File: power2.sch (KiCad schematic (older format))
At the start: 42 parts, among them U3 LMS6002DR2, U4 ECP5

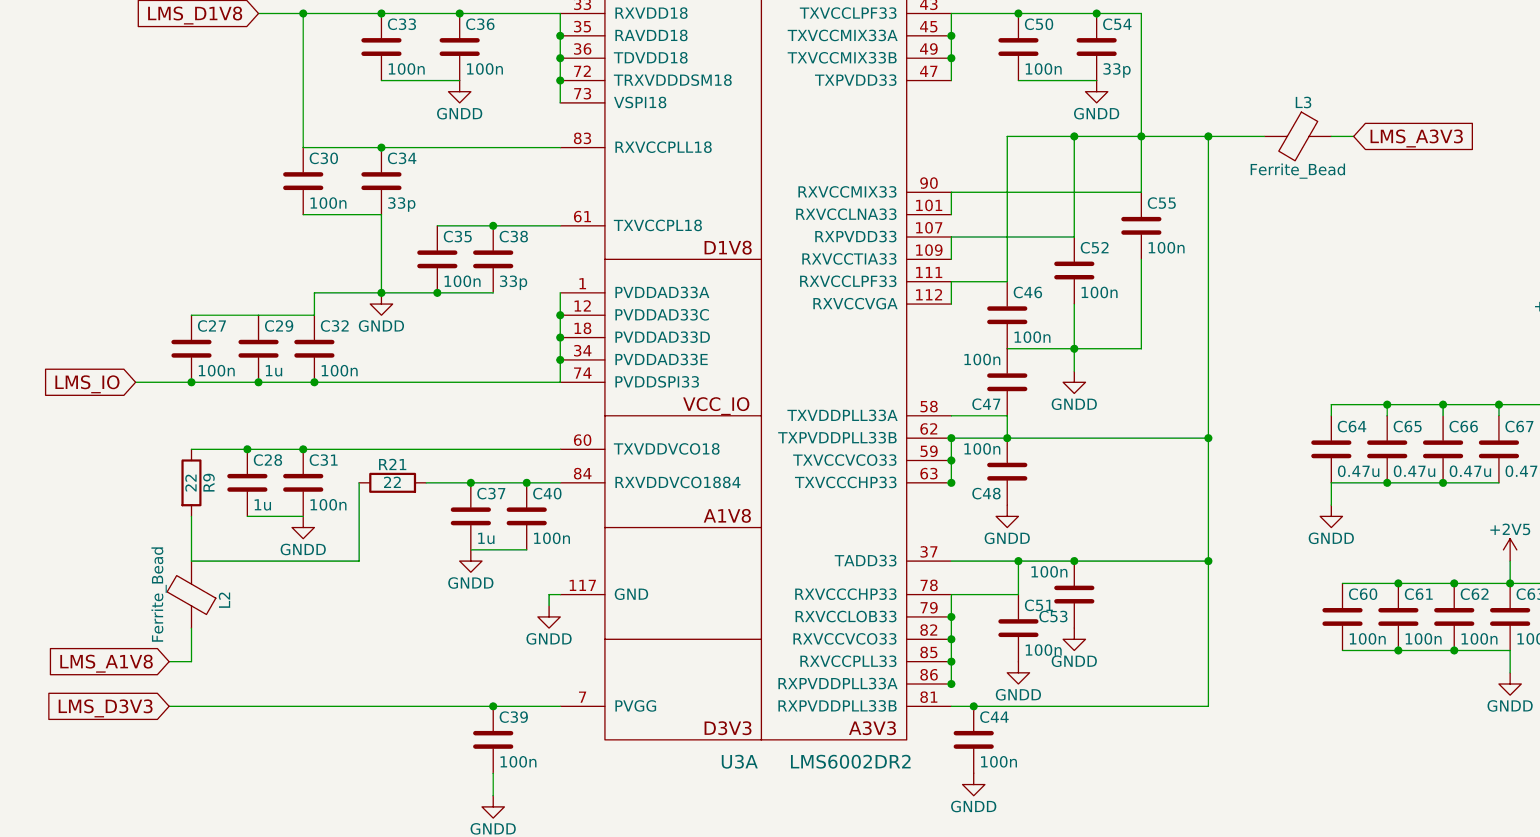
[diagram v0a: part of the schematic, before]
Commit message: Placed most components for FTDI. Begin tracing FT601
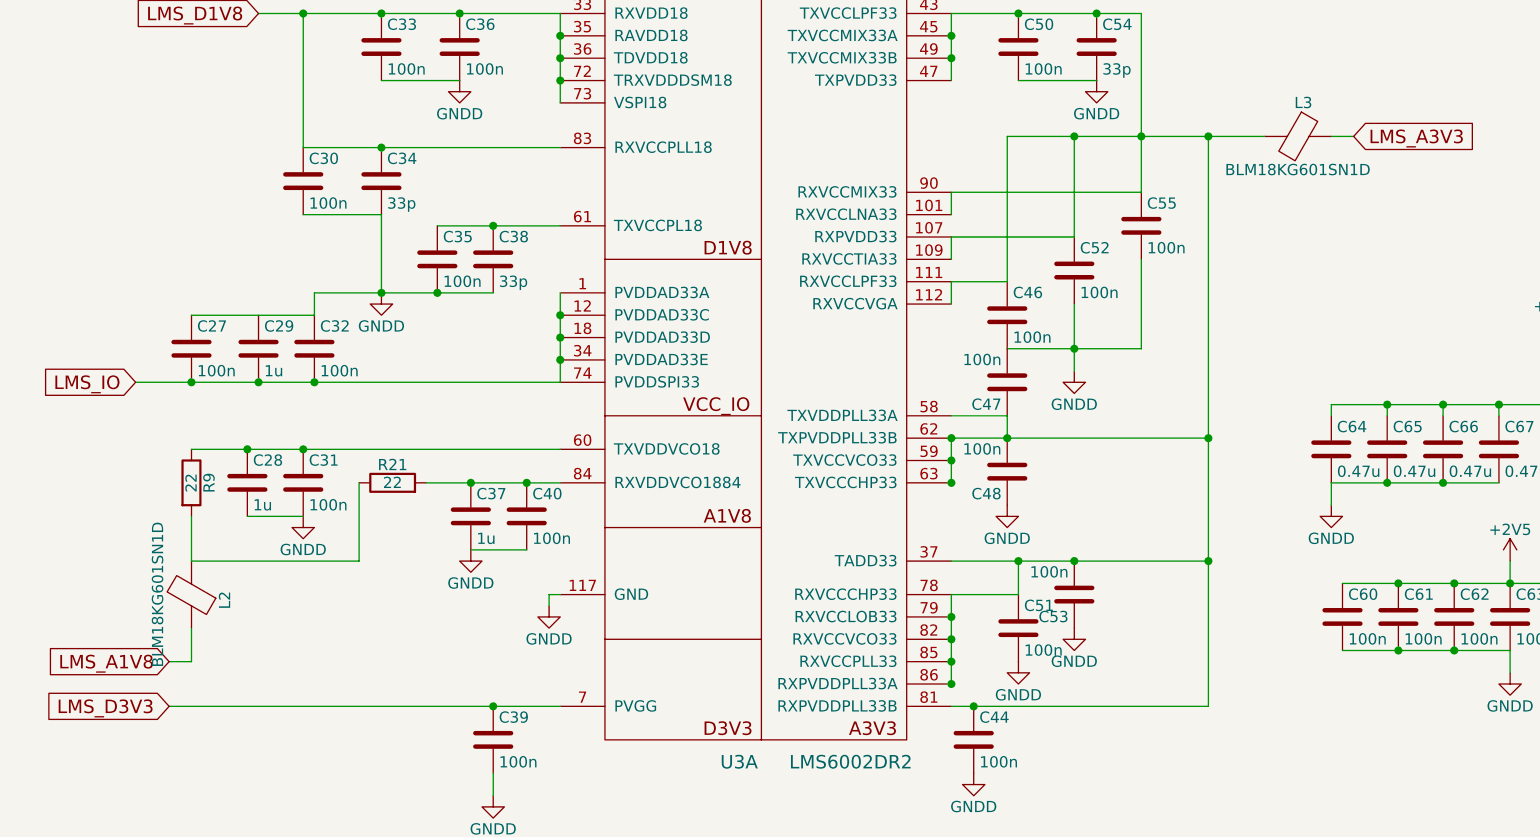
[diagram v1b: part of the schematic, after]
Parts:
- C27, C28, C29, C30, C31, C32, C33, C34, C35, C36, C37, C38, C39, C40, C44, C46, C47, C48, C50, C51, C52, C53, C54, C55, C60, C61, C62, C63, C64, C65, C66, C67, C68, C69, C70, C71: footprint Capacitors_SMD:C_0402 -> Capacitors_SMD:C_0603
- L2, L3: value Ferrite_Bead -> BLM18KG601SN1D; footprint Inductors_SMD:L_0603_HandSoldering -> Capacitors_SMD:C_0805
- R21, R9: footprint Resistors_SMD:R_0402 -> Resistors_SMD:R_0603

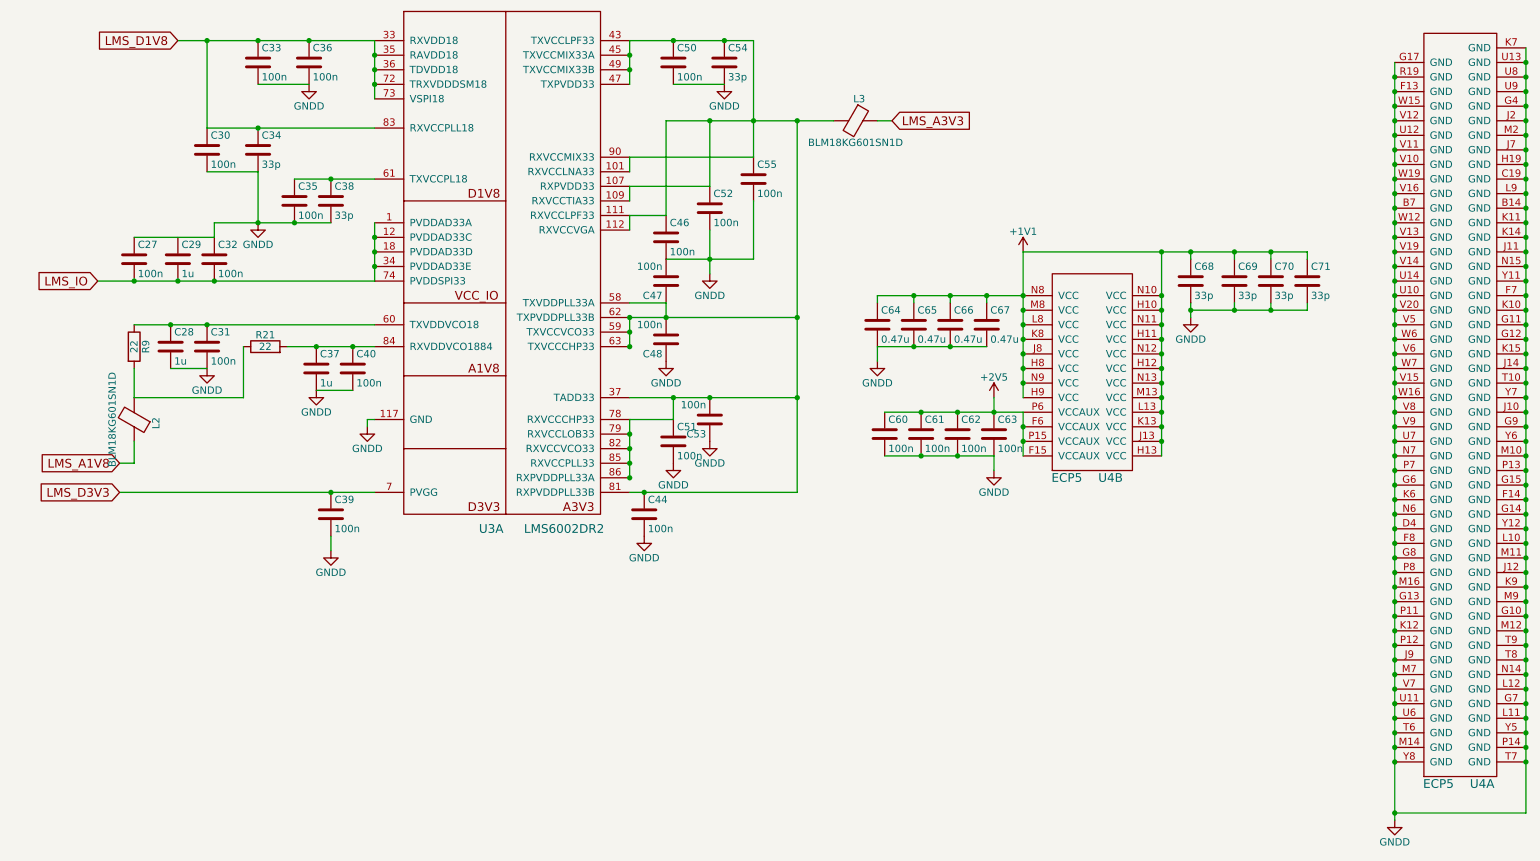
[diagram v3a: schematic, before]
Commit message: Start placing RF. Shield is ready. Fixed some net bugs.
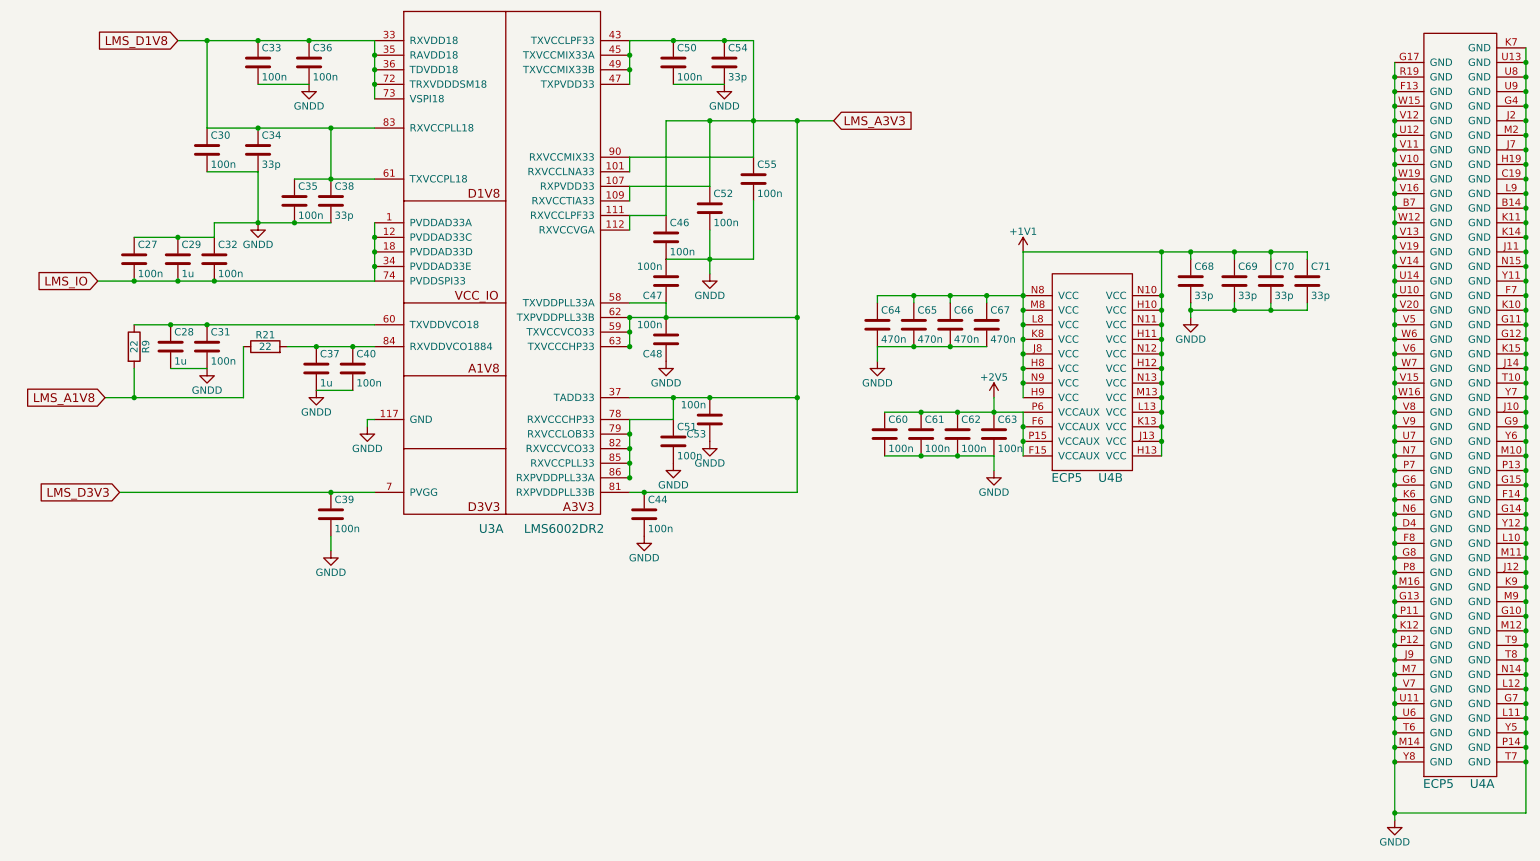
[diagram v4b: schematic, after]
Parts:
- removed L2, L3: BLM18KG601SN1D, Capacitors_SMD:C_0805, symbol Ferrite_Bead
- C64, C65, C66, C67: value 0.47u -> 470n
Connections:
- net GNDD: now also C29.1
- net LMS_A1V8: now also R21.1, R9.2
- net LMS_A3V3: now also C44.1, C46.1, C47.1, C48.2, C50.1, C51.1, C52.1, C53.2, C54.1, C55.1, U3.101 (RXVCCLNA33), U3.107 (RXPVDD33), U3.109 (RXVCCTIA33), U3.111 (RXVCCLPF33), U3.112 (RXVCCVGA), U3.37 (TADD33), U3.43 (TXVCCLPF33), U3.45 (TXVCCMIX33A), U3.47 (TXPVDD33), U3.49 (TXVCCMIX33B), U3.58 (TXVDDPLL33A), U3.59 (TXVCCVCO33), U3.62 (TXPVDDPLL33B), U3.63 (TXVCCCHP33), U3.78 (RXVCCCHP33), U3.79 (RXVCCLOB33), U3.81 (RXPVDDPLL33B), U3.82 (RXVCCVCO33), U3.85 (RXVCCPLL33), U3.86 (RXPVDDPLL33A), U3.90 (RXVCCMIX33)
- net LMS_D1V8: now also C35.1, C38.1, U3.61 (TXVCCPL18)
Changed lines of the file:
@@
 Connection ~ 10950 1000
 $Comp
-L GNDD #PWR058
+L GNDD #PWR067
 U 1 1 58A3CB56
 P 10050 6200
-F 0 "#PWR058" H 10050 5950 50  0001 C CNN
+F 0 "#PWR067" H 10050 5950 50  0001 C CNN
 F 1 "GNDD" H 10050 6050 50  0000 C CNN
 F 2 "" H 10050 6200 50  0000 C CNN
@@
 $EndComp
 $Comp
-L +1V1 #PWR059
+L +1V1 #PWR068
 U 1 1 58A3D047
 P 7500 2300
-F 0 "#PWR059" H 7500 2150 50  0001 C CNN
+F 0 "#PWR068" H 7500 2150 50  0001 C CNN
 F 1 "+1V1" H 7500 2440 50  0000 C CNN
 F 2 "" H 7500 2300 50  0000 C CNN
@@
 $EndComp
 $Comp
-L C C32
-U 1 1 58A43C54
-P 1950 2350
-F 0 "C32" H 1975 2450 50  0000 L CNN
-F 1 "100n" H 1975 2250 50  0000 L CNN
-F 2 "Capacitors_SMD:C_0603" H 1988 2200 50  0001 C CNN
-F 3 "" H 1950 2350 50  0000 C CNN
-	1    1950 2350
-	1    0    0    -1
-$EndComp
-$Comp
 L C C36
 U 1 1 58A43C5B
@@
 $EndComp
 $Comp
-L GNDD #PWR060
+L GNDD #PWR069
 U 1 1 58A43C7E
 P 2250 2100
-F 0 "#PWR060" H 2250 1850 50  0001 C CNN
+F 0 "#PWR069" H 2250 1850 50  0001 C CNN
 F 1 "GNDD" H 2250 1950 50  0000 C CNN
 F 2 "" H 2250 2100 50  0000 C CNN
@@
 LMS_D1V8
 $Comp
-L GNDD #PWR061
+L GNDD #PWR070
 U 1 1 58A43C85
 P 2600 1150
-F 0 "#PWR061" H 2600 900 50  0001 C CNN
+F 0 "#PWR070" H 2600 900 50  0001 C CNN
 F 1 "GNDD" H 2600 1000 50  0000 C CNN
 F 2 "" H 2600 1150 50  0000 C CNN
@@
 F 3 "" H 1400 2350 50  0000 C CNN
 	1    1400 2350
-	1    0    0    -1
-$EndComp
-$Comp
-L C C29
-U 1 1 58A43C92
-P 1700 2350
-F 0 "C29" H 1725 2450 50  0000 L CNN
-F 1 "1u" H 1725 2250 50  0000 L CNN
-F 2 "Capacitors_SMD:C_0603" H 1738 2200 50  0001 C CNN
-F 3 "" H 1700 2350 50  0000 C CNN
-	1    1700 2350
 	1    0    0    -1
 $EndComp
@@
 	1    0    0    -1
 $EndComp
-$Comp
-L Ferrite_Bead L2
-U 1 1 58A43CC3
-P 1400 3450
-F 0 "L2" V 1250 3475 50  0000 C CNN
-F 1 "BLM18KG601SN1D" V 1550 3450 50  0000 C CNN
-F 2 "Capacitors_SMD:C_0805" V 1330 3450 50  0001 C CNN
-F 3 "" H 1400 3450 50  0000 C CNN
-	1    1400 3450
-	-1   0    0    1
-$EndComp
-Text GLabel 1300 3750 0    60   Input ~ 0
+Text GLabel 1200 3300 0    60   Input ~ 0
 LMS_A1V8
 $Comp
-L GNDD #PWR062
+L GNDD #PWR071
 U 1 1 58A43CCB
 P 3000 3500
-F 0 "#PWR062" H 3000 3250 50  0001 C CNN
+F 0 "#PWR071" H 3000 3250 50  0001 C CNN
 F 1 "GNDD" H 3000 3350 50  0000 C CNN
 F 2 "" H 3000 3500 50  0000 C CNN
@@
 $EndComp
 $Comp
-L GNDD #PWR063
+L GNDD #PWR072
 U 1 1 58A43CD1
 P 2650 3250
-F 0 "#PWR063" H 2650 3000 50  0001 C CNN
+F 0 "#PWR072" H 2650 3000 50  0001 C CNN
 F 1 "GNDD" H 2650 3100 50  0000 C CNN
 F 2 "" H 2650 3250 50  0000 C CNN
@@
 $EndComp
 $Comp
-L GNDD #PWR064
+L GNDD #PWR073
 U 1 1 58A43CD7
 P 1900 3100
-F 0 "#PWR064" H 1900 2850 50  0001 C CNN
+F 0 "#PWR073" H 1900 2850 50  0001 C CNN
 F 1 "GNDD" H 1900 2950 50  0000 C CNN
 F 2 "" H 1900 3100 50  0000 C CNN
@@
 $EndComp
 $Comp
-L GNDD #PWR065
+L GNDD #PWR074
 U 1 1 58A43CEB
 P 5450 1150
-F 0 "#PWR065" H 5450 900 50  0001 C CNN
+F 0 "#PWR074" H 5450 900 50  0001 C CNN
 F 1 "GNDD" H 5450 1000 50  0000 C CNN
 F 2 "" H 5450 1150 50  0000 C CNN
@@
 	1    0    0    -1
 $EndComp
-$Comp
-L Ferrite_Bead L3
-U 1 1 58A43D06
-P 6350 1400
-F 0 "L3" V 6200 1425 50  0000 C CNN
-F 1 "BLM18KG601SN1D" V 6500 1400 50  0000 C CNN
-F 2 "Capacitors_SMD:C_0805" V 6280 1400 50  0001 C CNN
-F 3 "" H 6350 1400 50  0000 C CNN
-	1    6350 1400
-	0    1    1    0
-$EndComp
-Text GLabel 6600 1400 2    60   Input ~ 0
+Text GLabel 6200 1400 2    60   Input ~ 0
 LMS_A3V3
 $Comp
@@
 $EndComp
 $Comp
-L GNDD #PWR066
+L GNDD #PWR075
 U 1 1 58A43D15
 P 2750 4350
-F 0 "#PWR066" H 2750 4100 50  0001 C CNN
+F 0 "#PWR075" H 2750 4100 50  0001 C CNN
 F 1 "GNDD" H 2750 4200 50  0000 C CNN
 F 2 "" H 2750 4350 50  0000 C CNN
@@
 $EndComp
 $Comp
-L GNDD #PWR067
+L GNDD #PWR076
 U 1 1 58A43D1B
 P 5350 2450
-F 0 "#PWR067" H 5350 2200 50  0001 C CNN
+F 0 "#PWR076" H 5350 2200 50  0001 C CNN
 F 1 "GNDD" H 5350 2300 50  0000 C CNN
 F 2 "" H 5350 2450 50  0000 C CNN
@@
 $EndComp
 $Comp
-L GNDD #PWR068
+L GNDD #PWR077
 U 1 1 58A43D2F
 P 5050 3050
-F 0 "#PWR068" H 5050 2800 50  0001 C CNN
+F 0 "#PWR077" H 5050 2800 50  0001 C CNN
 F 1 "GNDD" H 5050 2900 50  0000 C CNN
 F 2 "" H 5050 3050 50  0000 C CNN
@@
 Connection ~ 3050 2200
 Wire Wire Line
-	1400 2200 1950 2200
-Wire Wire Line
 	1950 2200 1950 2100
 Connection ~ 2250 2100
@@
 Connection ~ 1900 2800
 Wire Wire Line
-	2150 2950 2150 3300
-Wire Wire Line
-	1300 3750 1400 3750
-Wire Wire Line
-	2150 3300 1400 3300
+	2150 3300 2150 2950
+Wire Wire Line
+	1200 3300 2150 3300
 Wire Wire Line
 	1400 3300 1400 3100
-Wire Wire Line
-	1400 3750 1400 3600
 Wire Wire Line
 	3000 3500 3000 3450
@@
 	5350 2150 5350 2450
 Connection ~ 5350 2350
-Wire Wire Line
-	6600 1400 6500 1400
 Wire Wire Line
 	5050 1400 6200 1400
@@
 Connection ~ 5350 3300
 $Comp
-L GNDD #PWR069
+L GNDD #PWR078
 U 1 1 58A43D94
 P 5350 3600
-F 0 "#PWR069" H 5350 3350 50  0001 C CNN
+F 0 "#PWR078" H 5350 3350 50  0001 C CNN
 F 1 "GNDD" H 5350 3450 50  0000 C CNN
 F 2 "" H 5350 3600 50  0000 C CNN
@@
 Connection ~ 5100 3300
 $Comp
-L GNDD #PWR070
+L GNDD #PWR079
 U 1 1 58A43DAE
 P 5100 3750
-F 0 "#PWR070" H 5100 3500 50  0001 C CNN
+F 0 "#PWR079" H 5100 3500 50  0001 C CNN
 F 1 "GNDD" H 5100 3600 50  0000 C CNN
 F 2 "" H 5100 3750 50  0000 C CNN
@@
 $EndComp
 $Comp
-L GNDD #PWR071
+L GNDD #PWR080
 U 1 1 58A43DB4
 P 4900 4250
-F 0 "#PWR071" H 4900 4000 50  0001 C CNN
+F 0 "#PWR080" H 4900 4000 50  0001 C CNN
 F 1 "GNDD" H 4900 4100 50  0000 C CNN
 F 2 "" H 4900 4250 50  0000 C CNN
@@
 	7500 2300 9450 2300
 $Comp
-L +2V5 #PWR072
+L +2V5 #PWR081
 U 1 1 58A517A0
 P 7300 3300
-F 0 "#PWR072" H 7300 3150 50  0001 C CNN
+F 0 "#PWR081" H 7300 3150 50  0001 C CNN
 F 1 "+2V5" H 7300 3440 50  0000 C CNN
 F 2 "" H 7300 3300 50  0000 C CNN
@@
 $EndComp
 $Comp
-L GNDD #PWR073
+L GNDD #PWR082
 U 1 1 58A51D8C
 P 7300 3800
-F 0 "#PWR073" H 7300 3550 50  0001 C CNN
+F 0 "#PWR082" H 7300 3550 50  0001 C CNN
 F 1 "GNDD" H 7300 3650 50  0000 C CNN
 F 2 "" H 7300 3800 50  0000 C CNN
@@
 P 7250 2800
 F 0 "C67" H 7275 2900 50  0000 L CNN
-F 1 "0.47u" H 7275 2700 50  0000 L CNN
+F 1 "470n" H 7275 2700 50  0000 L CNN
 F 2 "Capacitors_SMD:C_0603" H 7288 2650 50  0001 C CNN
 F 3 "" H 7250 2800 50  0000 C CNN
@@
 P 7000 2800
 F 0 "C66" H 7025 2900 50  0000 L CNN
-F 1 "0.47u" H 7025 2700 50  0000 L CNN
+F 1 "470n" H 7025 2700 50  0000 L CNN
 F 2 "Capacitors_SMD:C_0603" H 7038 2650 50  0001 C CNN
 F 3 "" H 7000 2800 50  0000 C CNN
@@
 P 6750 2800
 F 0 "C65" H 6775 2900 50  0000 L CNN
-F 1 "0.47u" H 6775 2700 50  0000 L CNN
+F 1 "470n" H 6775 2700 50  0000 L CNN
 F 2 "Capacitors_SMD:C_0603" H 6788 2650 50  0001 C CNN
 F 3 "" H 6750 2800 50  0000 C CNN
@@
 P 6500 2800
 F 0 "C64" H 6525 2900 50  0000 L CNN
-F 1 "0.47u" H 6525 2700 50  0000 L CNN
+F 1 "470n" H 6525 2700 50  0000 L CNN
 F 2 "Capacitors_SMD:C_0603" H 6538 2650 50  0001 C CNN
 F 3 "" H 6500 2800 50  0000 C CNN
@@
 Connection ~ 6750 2950
 $Comp
-L GNDD #PWR074
+L GNDD #PWR083
 U 1 1 58A54D9A
 P 6500 3050
-F 0 "#PWR074" H 6500 2800 50  0001 C CNN
+F 0 "#PWR083" H 6500 2800 50  0001 C CNN
 F 1 "GNDD" H 6500 2900 50  0000 C CNN
 F 2 "" H 6500 3050 50  0000 C CNN
@@
 $EndComp
 Wire Wire Line
-	9450 2650 9450 2700
-Wire Wire Line
-	9450 2700 8650 2700
+	9450 2700 9450 2650
+Wire Wire Line
+	8650 2700 9450 2700
 Wire Wire Line
 	8650 2650 8650 2750
@@
 Connection ~ 8650 2300
 $Comp
-L GNDD #PWR075
+L GNDD #PWR084
 U 1 1 58A55DE2
 P 8650 2750
-F 0 "#PWR075" H 8650 2500 50  0001 C CNN
+F 0 "#PWR084" H 8650 2500 50  0001 C CNN
 F 1 "GNDD" H 8650 2600 50  0000 C CNN
 F 2 "" H 8650 2750 50  0000 C CNN
@@
 $EndComp
 Connection ~ 8650 2700
+Connection ~ 1400 3300
+Wire Wire Line
+	2750 1800 2750 1450
+Connection ~ 2750 1450
+$Comp
+L C C29
+U 1 1 58A43C92
+P 1700 2350
+F 0 "C29" H 1725 2450 50  0000 L CNN
+F 1 "1u" H 1725 2250 50  0000 L CNN
+F 2 "Capacitors_SMD:C_0603" H 1738 2200 50  0001 C CNN
+F 3 "" H 1700 2350 50  0000 C CNN
+	1    1700 2350
+	1    0    0    -1
+$EndComp
+$Comp
+L C C32
+U 1 1 58A43C54
+P 1950 2350
+F 0 "C32" H 1975 2450 50  0000 L CNN
+F 1 "100n" H 1975 2250 50  0000 L CNN
+F 2 "Capacitors_SMD:C_0603" H 1988 2200 50  0001 C CNN
+F 3 "" H 1950 2350 50  0000 C CNN
+	1    1950 2350
+	1    0    0    -1
+$EndComp
+Wire Wire Line
+	1400 2200 1950 2200
+Connection ~ 1700 2200
 $EndSCHEMATC
